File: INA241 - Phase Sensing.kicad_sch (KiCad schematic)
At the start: 48 parts, among them IC10 INA241A2IDGKR, IC2 INA241A2IDGKR, IC4 INA241A2IDGKR, IC6 INA241A2IDGKR

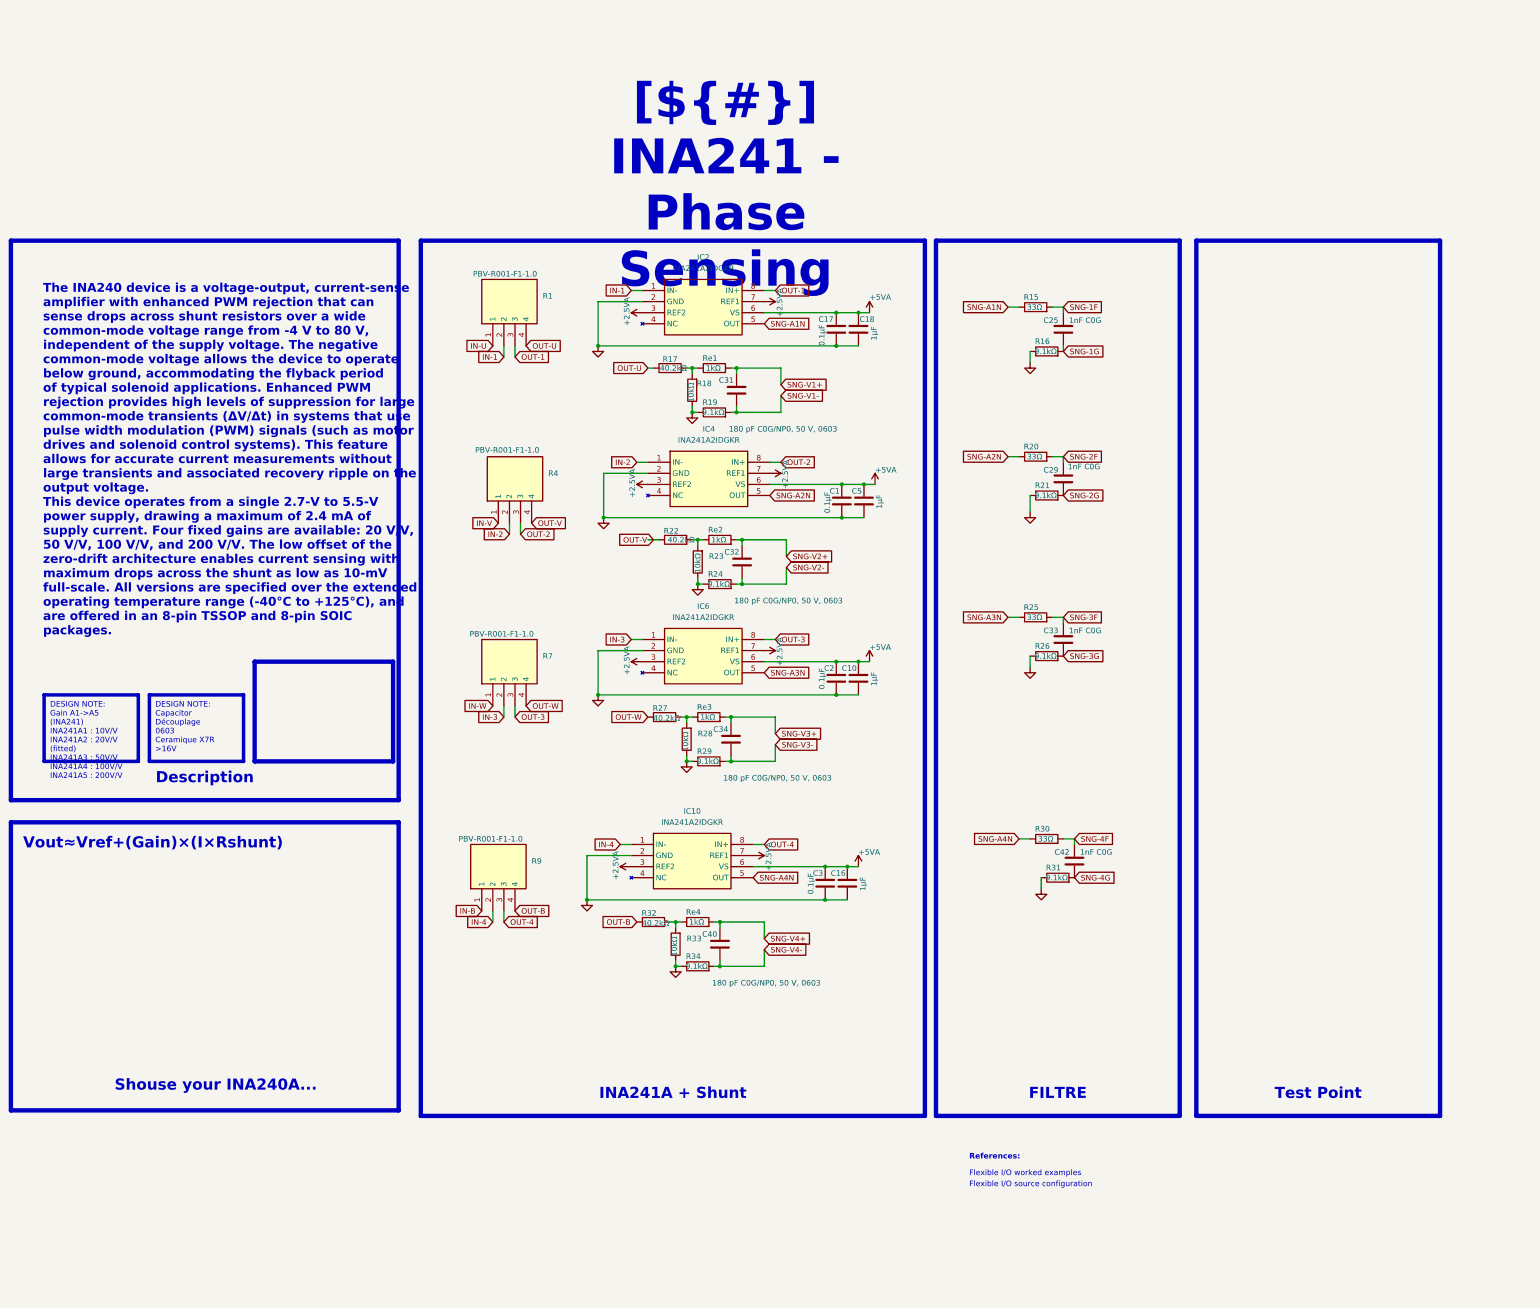
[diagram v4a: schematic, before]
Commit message: Restyle schematic sheets, new title block logo, WE-MAPI inductor in simulations
- Schematic sheets: restyled frames, tables and text boxes
- Title block: INGENIERIE FRANCE logo in KDT_Template_GIT.kicad_wks
- LTspice: L1 modelled as WE-MAPI 4030 74438357022 (22 mOhm),
  simulations 01 and 03 rerun, README and results updated

Co-Authored-By: Claude Opus 5.5 <noreply@anthropic.com>
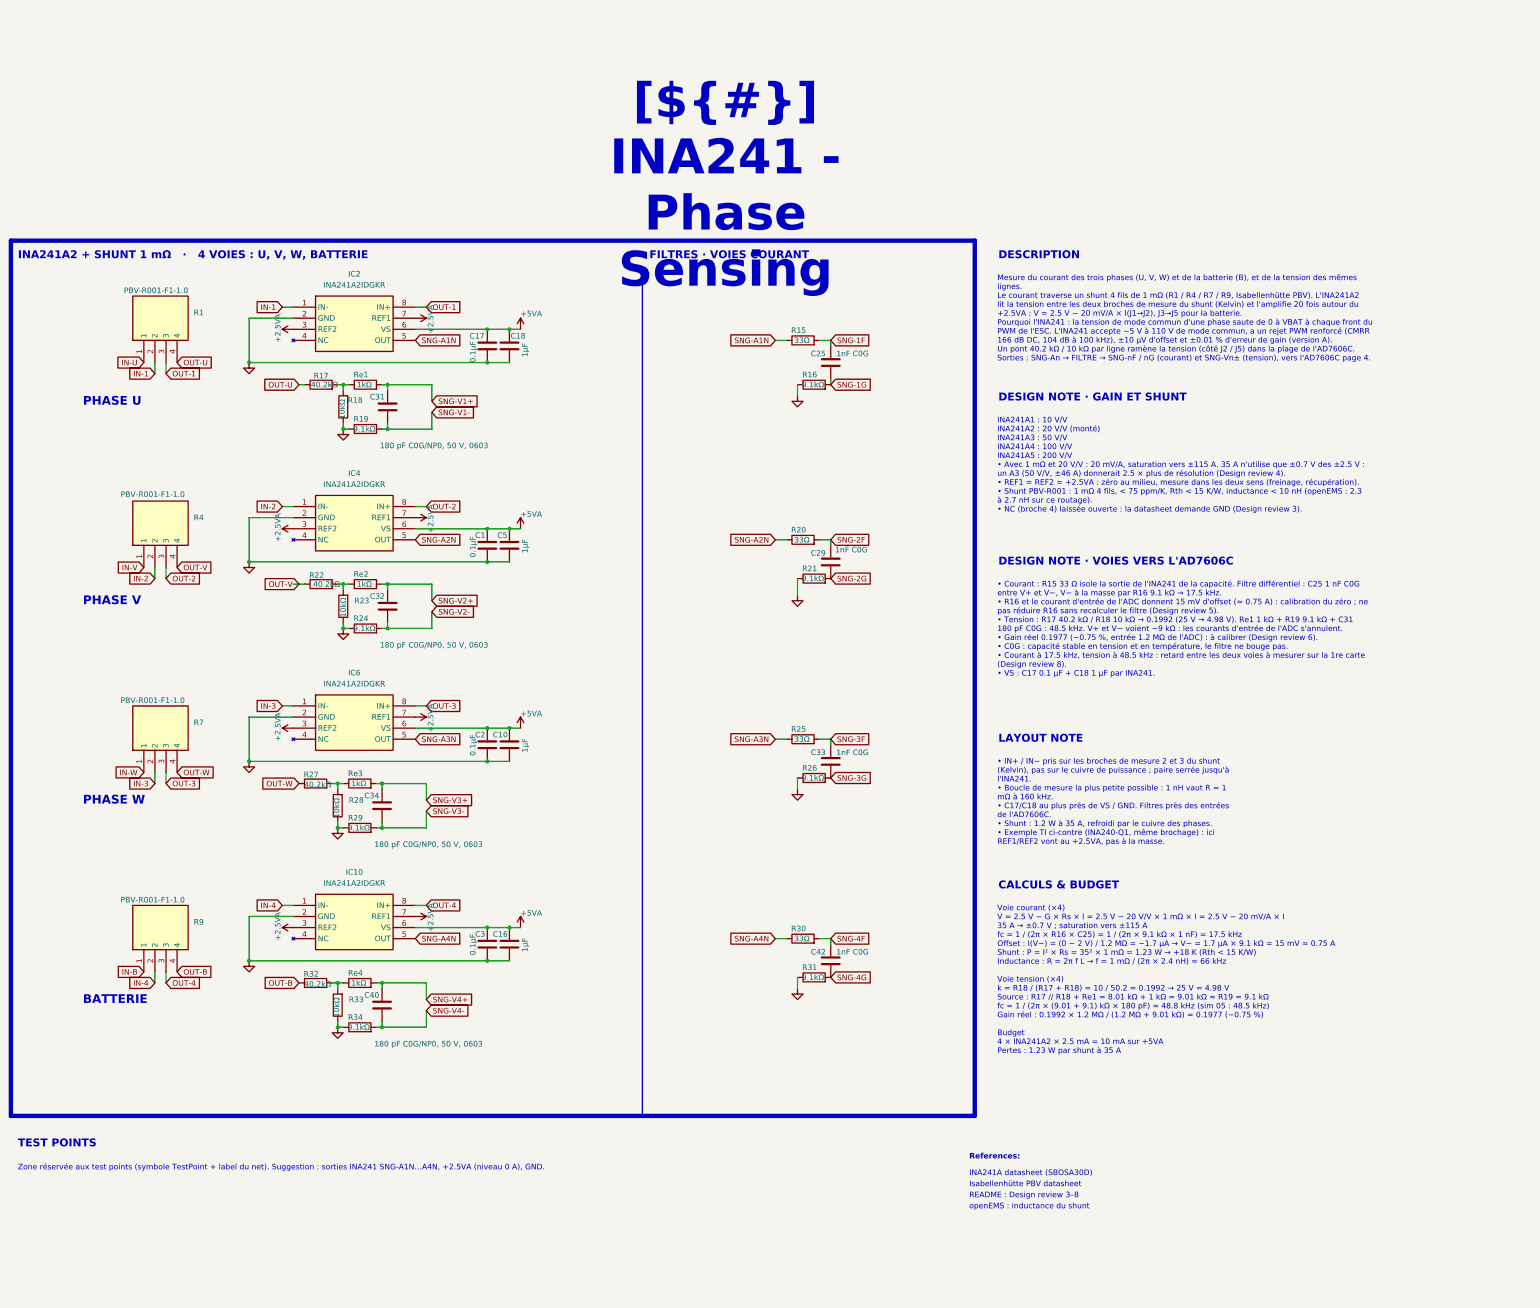
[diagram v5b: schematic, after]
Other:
- note added: "BATTERIE"
- note added: "INA241A datasheet (SBOSA30D)"
- note added: "Isabellenhütte PBV datasheet"
- note added: "PHASE U"
- note added: "PHASE V"
- note added: "PHASE W"
- note added: "README : Design review 3–8"
- note added: "openEMS : inductance du shunt"
- note removed: "Flexible I/O source configuration"
- note removed: "Flexible I/O worked examples"
- note removed: "The INA240 device is a voltage-output, current-sense amplifier with enhanced PWM rejection that can sense drops across shunt resistors over a wide common-mode voltage range from -4 V to 80 V, independent of the supply voltage. The negative common-mode voltage allows the device to operate below ground, accommodating the flyback period of typical solenoid applications. Enhanced PWM rejection provid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"
- note removed: "Vout≈Vref+(Gain)×(I×Rshunt)"
- moved on the sheet: C1, C10, C16, C17, C18, C2, C25, C29, C3, C31, C32, C33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

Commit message: Wire the AD7606C-18 digital side to host header J4, add test points
- AD7606C-18: software mode (OS0-2 high), serial (PAR/SER SEL high),
  REF SELECT low; CONVST, BUSY, RESET, CS, SCLK, SDI, FRSTDATA and
  DOUTA-D to J4 (2x8 pin header 2.54 mm, horizontal), +3.3V on J4 pin 1
- AD7606C-18 AGND pin 26 and REFGND pin 46 on GND
- Test points TP1-TP16: rails, INA241 outputs, CONVST, BUSY
- Nets renamed SHUNT_*, INA_*, ADC_*; net colours in the project
- LT3045-1 footprint: thermal vias numbered as exposed pad 13
- PCB updated from the schematic; ADC_* digital nets not routed yet
- README template / CHANGELOG: status, J4 pinout, design review 1 and 2
  fixed, new finding 9 (VDRIVE above AVCC + 0.3 V at power-up),
  4 channels / 8 ADC inputs

Co-Authored-By: Claude Opus 5.5 <noreply@anthropic.com>
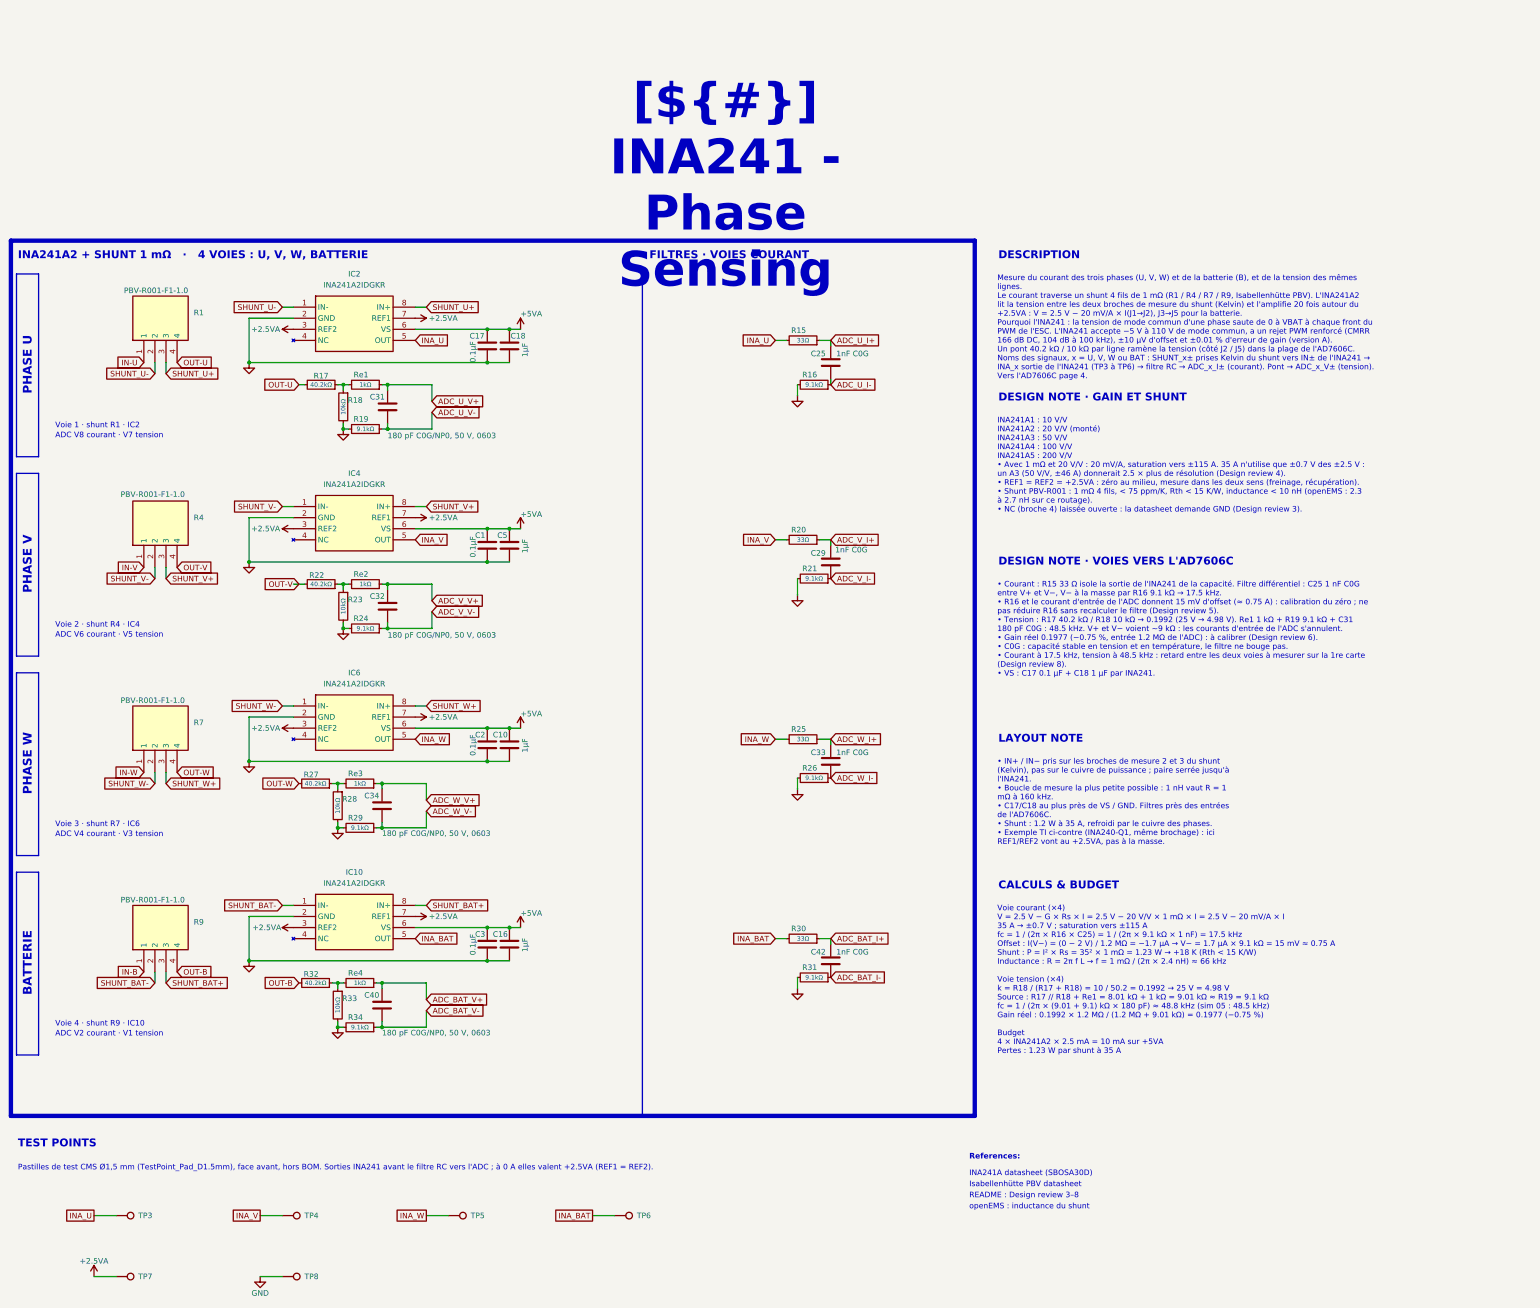
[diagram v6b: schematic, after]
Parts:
- added TP3, TP4, TP5, TP6, TP7, TP8: TestPoint, OPEN_PHASE:TestPoint_Pad_D1.5mm, symbol OPEN_PHASE:TestPoint
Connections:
- net +2.5VA: now also TP7.1
- net GND: now also TP8.1
- net IN-1 renamed SHUNT_U-
- net IN-2 renamed SHUNT_V-
- net IN-3 renamed SHUNT_W-
- net IN-4 renamed SHUNT_BAT-
- net OUT-1 renamed SHUNT_U+
- net OUT-2 renamed SHUNT_V+
- net OUT-3 renamed SHUNT_W+
- net OUT-4 renamed SHUNT_BAT+
- net SNG-1F renamed ADC_U_I+
- net SNG-1G renamed ADC_U_I-
- net SNG-2F renamed ADC_V_I+
- net SNG-2G renamed ADC_V_I-
- net SNG-3F renamed ADC_W_I+
- net SNG-3G renamed ADC_W_I-
- net SNG-4F renamed ADC_BAT_I+
- net SNG-4G renamed ADC_BAT_I-
- net SNG-A1N renamed INA_U
- net INA_U: now also TP3.1
- net SNG-A2N renamed INA_V
- net INA_V: now also TP4.1
- net SNG-A3N renamed INA_W
- net INA_W: now also TP5.1
- net SNG-A4N renamed INA_BAT
- net INA_BAT: now also TP6.1
- net SNG-V1+ renamed ADC_U_V+
- net SNG-V1- renamed ADC_U_V-
- net SNG-V2+ renamed ADC_V_V+
- net SNG-V2- renamed ADC_V_V-
- net SNG-V3+ renamed ADC_W_V+
- net SNG-V3- renamed ADC_W_V-
- net SNG-V4+ renamed ADC_BAT_V+
- net SNG-V4- renamed ADC_BAT_V-
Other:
- note added: "ADC V2 courant · V1 tension"
- note added: "ADC V4 courant · V3 tension"
- note added: "ADC V6 courant · V5 tension"
- note added: "ADC V8 courant · V7 tension"
- note added: "Voie 1 · shunt R1 · IC2"
- note added: "Voie 2 · shunt R4 · IC4"
- note added: "Voie 3 · shunt R7 · IC6"
- note added: "Voie 4 · shunt R9 · IC10"
